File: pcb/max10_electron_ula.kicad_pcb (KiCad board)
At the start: 4 copper layers, 55 x 89 mm, 83 parts

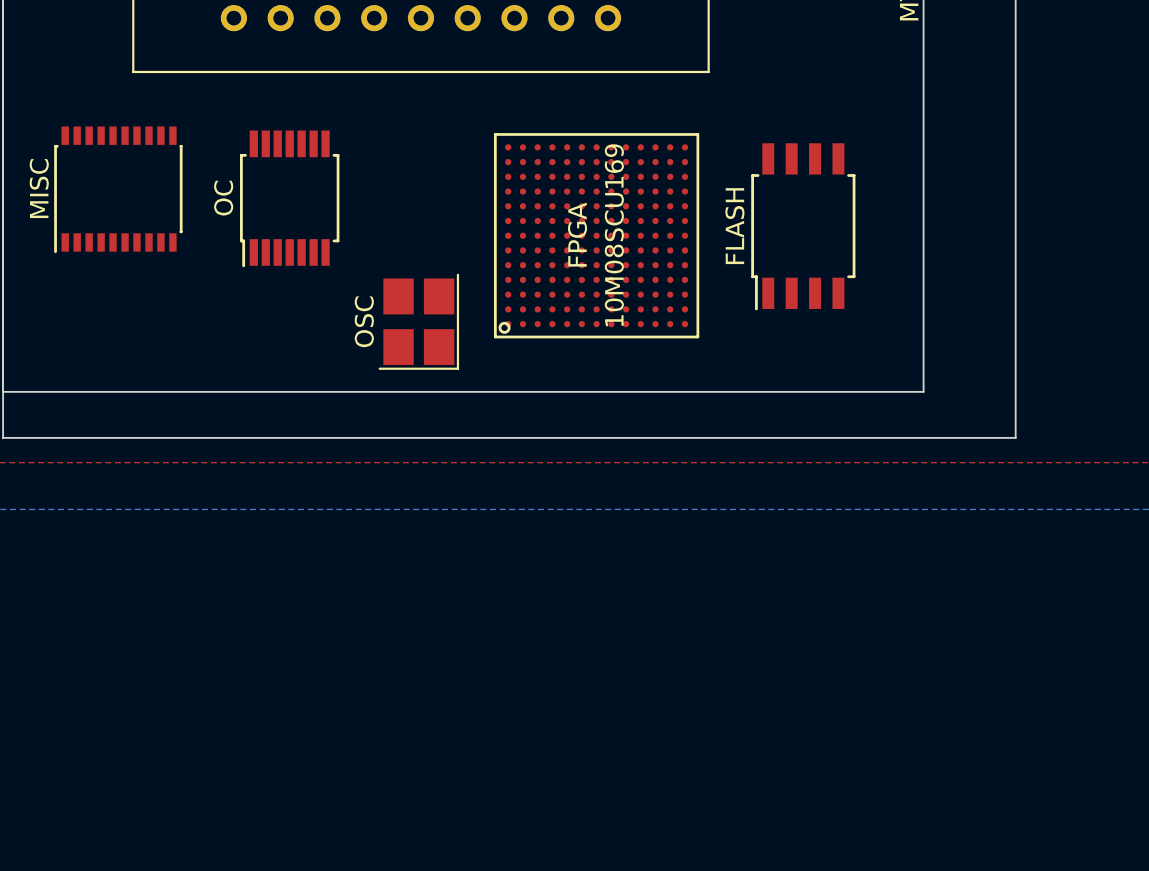
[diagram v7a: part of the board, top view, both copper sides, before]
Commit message: Fan out for FPGA more or less done -- time to assign pins
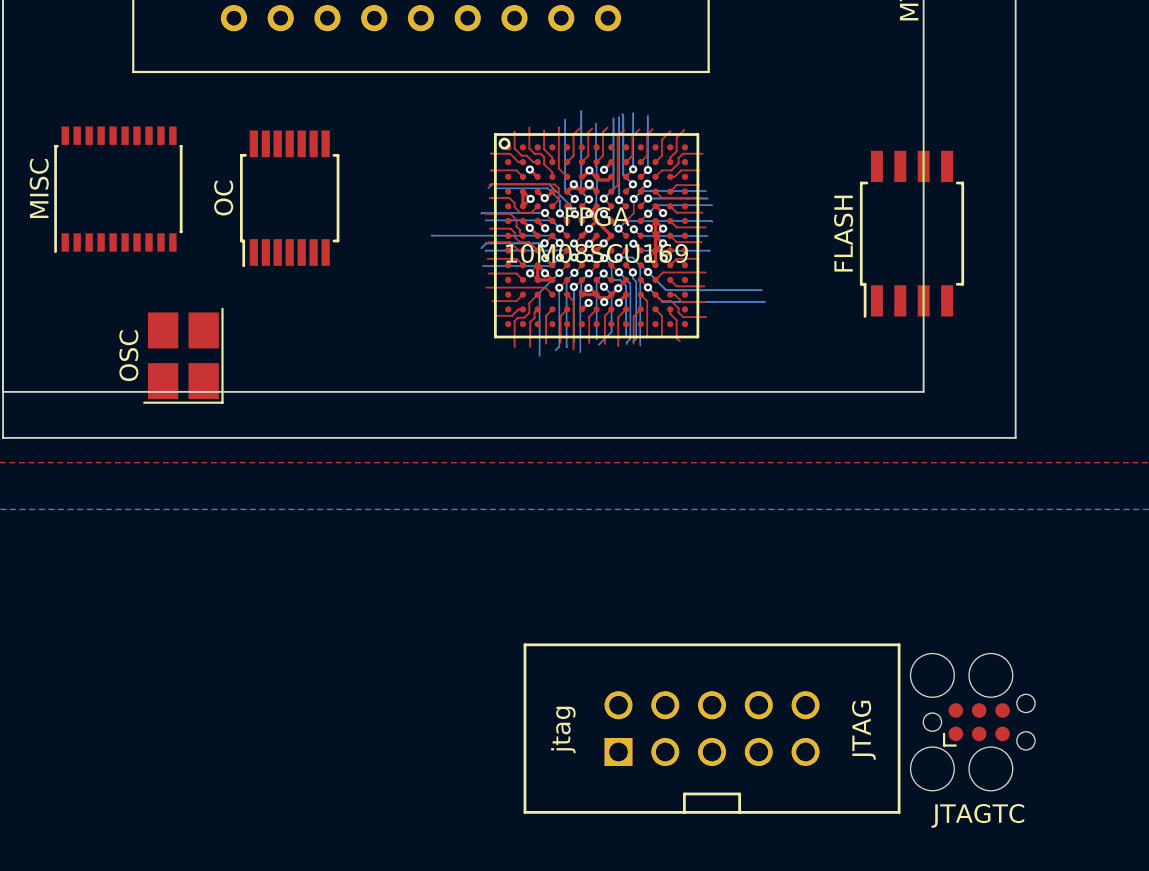
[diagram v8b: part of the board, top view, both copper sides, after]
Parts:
- added JTAG: jtag, myelin-kicad:jtag_shrouded_2x5, F.Cu at (185.7, 122.2)
- added JTAGTC: jtagtc, Tag-Connect_TC2030-IDC-FP_2x03_P1.27mm_Vertical, F.Cu at (200.2, 121.9)
- moved OSC 12.9 mm to (157.0, 102.0)
- moved FLASH 5.92 mm to (196.6, 95.3)
- turned FPGA to 0 degrees
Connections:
- net C1_1 renamed conn21
- net C1_11 renamed conn0
- net C1_12 renamed conn43
- net C1_13 renamed conn41
- net C1_14 renamed conn2
- net C1_16 renamed conn6
- net C1_17 renamed conn4
- net C1_18 renamed conn42
- net C1_19 renamed conn3
- net C1_2 renamed conn20
- net C1_20 renamed conn7
- net C1_22 renamed conn62
- net C1_23 renamed conn5
- net C1_24 renamed conn44
- net C1_25 renamed conn9
- net C1_26 renamed conn8
- net C1_27 renamed conn63
- net C1_28 renamed conn77
- net C1_29 renamed conn64
- net C1_3 renamed conn25
- net C1_30 renamed conn10
- net C1_31 renamed conn45
- net C1_33 renamed conn30
- net C1_34 renamed conn65
- net C1_36 renamed conn29
- net C1_37 renamed conn31
- net C1_38 renamed conn66
- net C1_5 renamed conn39
- net C1_6 renamed conn38
- net C1_7 renamed conn57
- net C1_9 renamed conn1
- net C2_1 renamed conn22
- net C2_12 renamed conn27
- net C2_3 renamed conn78
- net C2_4 renamed conn56
- net C2_5 renamed conn23
- net C2_8 renamed conn24
- net C3_1 renamed conn68
- net C3_10 renamed conn34
- net C3_11 renamed conn74
- net C3_12 renamed conn72
- net C3_2_CLK3n renamed conn111
- net C3_3 renamed conn67
- net C3_4 renamed conn32
- net C3_5_CLK3p renamed conn112
- net C3_6 renamed conn69
- net C3_7 renamed conn71
- net C3_8 renamed conn70
- net C3_9 renamed conn73
- net C4_10 renamed conn61
- net C4_11 renamed conn46
- net C4_12 renamed conn28
- net C4_13 renamed conn47
- net C4_14 renamed conn48
- net C4_15_DPCLK1 renamed conn114
- net C4_16_DPCLK0 renamed conn113
- net C4_17 renamed conn11
- net C4_18 renamed conn79
- net C4_19 renamed conn12
- net C4_20 renamed conn49
- net C4_22 renamed conn15
- net C4_23 renamed conn51
- net C4_24 renamed conn13
- net C4_25 renamed conn14
- net C4_26 renamed conn17
- net C4_27 renamed conn53
- net C4_28 renamed conn16
- net C4_30 renamed conn54
- net C4_31 renamed conn18
- net C4_32 renamed conn76
- net C4_33 renamed conn52
- net C4_34 renamed conn33
- net C4_35 renamed conn35
- net C4_36 renamed conn19
- net C4_37 renamed conn36
- net C4_38 renamed conn55
- net C4_39 renamed conn37
- net C4_3_VREFB2N0 renamed conn117
- net C4_4 renamed conn26
- net C4_40 renamed conn75
- net C4_6 renamed conn60
- net C4_7 renamed conn58
- net C4_8 renamed conn59
- net CLK0n renamed conn105
- net CLK0p renamed conn106
- net CLK1n renamed conn107
- net CLK1p renamed conn108
- net CLK2n renamed conn109
- net CLK2p renamed conn110
- net DPCLK2 renamed conn115
- net DPCLK3 renamed conn116
- FPGA pad B4: C1_10 -> conn40
- FPGA pad D9: (no net) -> conn80
- FPGA pad E10: (no net) -> conn84
- FPGA pad E4: (no net) -> conn81
- FPGA pad E6: (no net) -> conn82
- FPGA pad E8: (no net) -> conn83
- FPGA pad E9: (no net) -> conn95
- FPGA pad F4: (no net) -> conn96
- FPGA pad F8: (no net) -> conn85
- FPGA pad G4: (no net) -> conn86
- FPGA pad H10: (no net) -> conn98
- FPGA pad H3: (no net) -> conn104
- FPGA pad H8: (no net) -> conn87
- FPGA pad H9: (no net) -> conn97
- FPGA pad J10: (no net) -> conn90
- FPGA pad J5: (no net) -> conn88
- FPGA pad J6: (no net) -> conn89
- FPGA pad J7: (no net) -> conn99
- FPGA pad J8: (no net) -> conn100
- FPGA pad J9: (no net) -> conn101
- FPGA pad K10: (no net) -> conn93
- FPGA pad K5: (no net) -> conn102
- FPGA pad K6: (no net) -> conn103
- FPGA pad K7: (no net) -> conn91
- FPGA pad K8: (no net) -> conn92
- FPGA pad L4: (no net) -> conn94
- FPGA pad M7: C4_21 -> conn40
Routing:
- net 3V3: track 0.00 -> 28.1 mm, vias 0 -> 18
- net GND: track 0.00 -> 11.3 mm, vias 0 -> 12
- net conn108: track 0.00 -> 7.70 mm, vias 0 -> 1
- net conn93: track 0.00 -> 7.24 mm, vias 0 -> 1
- net conn90: track 0.00 -> 7.13 mm, vias 0 -> 1
- net conn97: track 0.00 -> 6.28 mm, vias 0 -> 1
- net fpga_TDO: track 0.00 -> 6.12 mm, vias 0 -> 1
- net conn110: track 0.00 -> 5.84 mm, vias 0 -> 1
- net conn85: track 0.00 -> 5.68 mm, vias 0 -> 1
- net conn87: track 0.00 -> 5.55 mm, vias 0 -> 1
- net conn106: track 0.00 -> 5.55 mm, vias 0 -> 1
- net conn88: track 0.00 -> 5.55 mm, vias 0 -> 1
- net conn82: track 0.00 -> 5.50 mm, vias 0 -> 1
- net conn116: track 0.00 -> 5.47 mm, vias 0 -> 1
- net conn83: track 0.00 -> 5.16 mm, vias 0 -> 1
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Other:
- net class Power: via_dia 0.6 -> 0.51; via_drill 0.3 -> 0.25
